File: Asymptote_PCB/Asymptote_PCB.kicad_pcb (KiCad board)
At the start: 2 copper layers, 241.3 x 74.6 mm, 107 parts, among them J1 XIAO nrf52840, J4 Conn_01x03_Female, J5 Conn_01x02_Female, SW1 MX_SW_solder, SW10 MX_SW_solder, SW11 MX_SW_solder, SW12 MX_SW_solder, SW13 MX_SW_solder, SW14 MX_SW_solder, SW15 MX_SW_solder, SW16 MX_SW_solder, SW17 MX_SW_solder, SW18 MX_SW_solder, SW19 MX_SW_solder, SW2 MX_SW_solder, SW20 MX_SW_solder, SW21 MX_SW_solder, SW22 MX_SW_solder, SW23 MX_SW_solder, SW24 MX_SW_solder, SW25 MX_SW_solder, SW26 MX_SW_solder, SW27 MX_SW_solder, SW28 MX_SW_solder, SW29 MX_SW_solder, SW3 MX_SW_solder, SW30 MX_SW_solder, SW31 MX_SW_solder, SW32 MX_SW_solder, SW33 MX_SW_solder, SW34 MX_SW_solder, SW35 MX_SW_solder, SW36 MX_SW_solder, SW37 MX_SW_solder, SW38 MX_SW_solder, SW39 MX_SW_solder, SW4 MX_SW_solder, SW40 MX_SW_solder, SW41 MX_SW_solder, SW42 MX_SW_solder, SW43 MX_SW_solder, SW44 MX_SW_solder, SW45 MX_SW_solder, SW46 MX_SW_solder, SW47 MX_SW_solder, SW48 MX_SW_solder, SW49 MX_SW_solder, SW5 MX_SW_solder, SW50 MX_SW_solder, SW51 MX_SW_solder, SW6 MX_SW_solder, SW7 MX_SW_solder, SW8 MX_SW_solder, SW9 MX_SW_solder

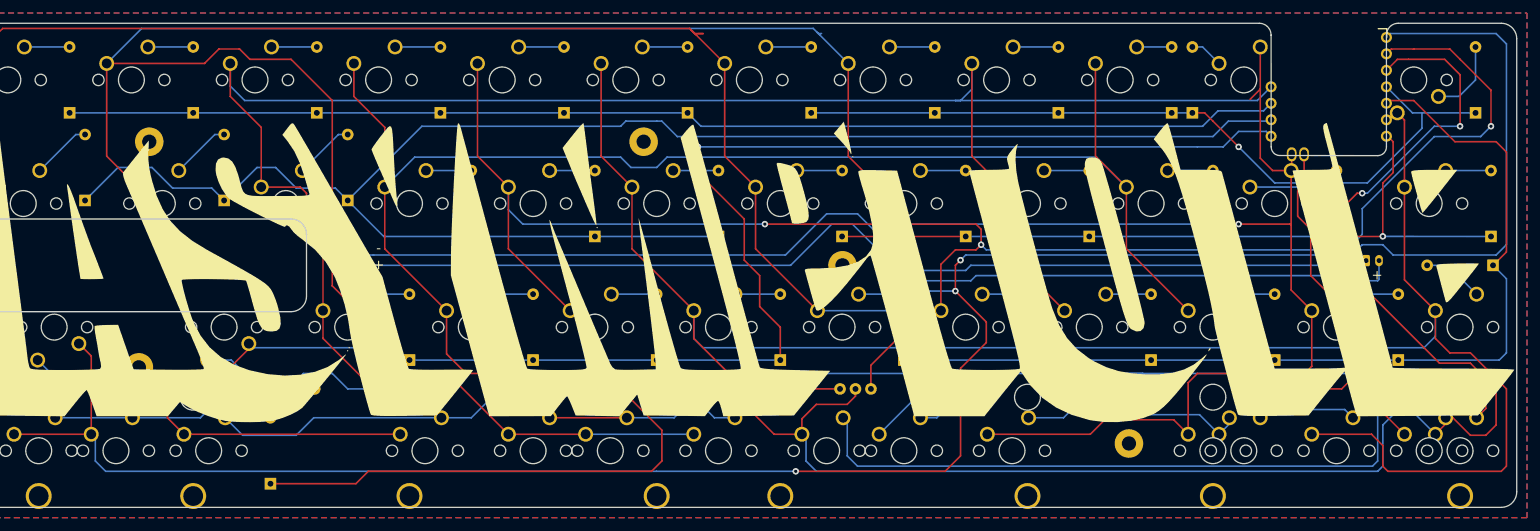
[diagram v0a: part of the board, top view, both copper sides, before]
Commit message: Added 7u stab holes, V2 Gerbers
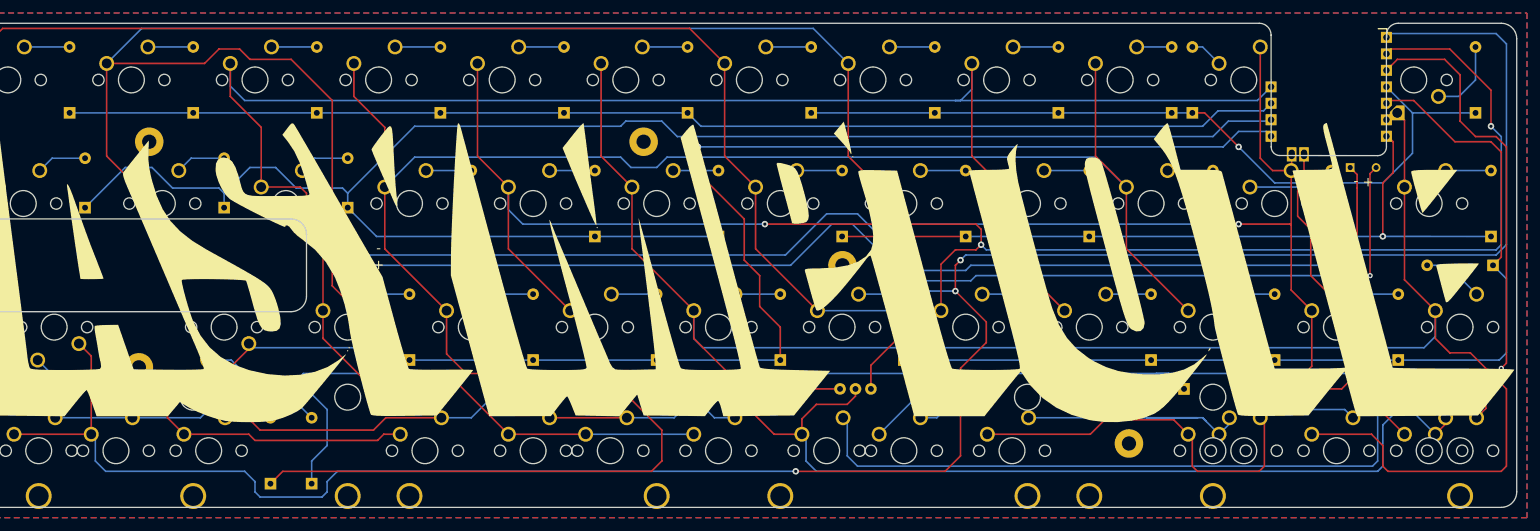
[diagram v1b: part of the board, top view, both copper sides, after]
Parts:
- added S5: MX_stab, marbastlib-mx:STAB_MX_P_7u, F.Cu at (144.5, 109.5)
- D13, D14, D15: footprint Diode_THT:D_A-405_P10.16mm_Horizontal -> Diode_THT:D_A-405_P7.62mm_Horizontal
- J4: footprint Connector_JST:JST_PH_S3B-PH-K_1x03_P2.00mm_Horizontal -> Connector_PinHeader_2.00mm:PinHeader_1x03_P2.00mm_Vertical
- J5: footprint Connector_JST:JST_PH_S2B-PH-K_1x02_P2.00mm_Horizontal -> Connector_PinHeader_2.00mm:PinHeader_1x03_P2.00mm_Vertical
- moved D26 18.1 mm to (81.8, 114.6), turned to 90 degrees
- moved J5 14.5 mm to (241.8, 65.9), turned to -90 degrees
- moved J4 5.38 mm to (86.5, 78.2), turned to 180 degrees
- moved D41 3.97 mm to (216.2, 100.0)
- moved D13 1.11 mm to (46.8, 72.1)
- moved D14 1.11 mm to (68.3, 72.1)
- moved D15 1.11 mm to (87.3, 72.1)
- moved D23 0.79 mm to (238.9, 76.5)
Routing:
- net COL3: track 503.7 -> 477.2 mm, vias 2 -> 1
- net ROW4: track 207.5 -> 225.2 mm
- net +BATT: track 168.8 -> 182.5 mm, vias 0 -> 1
- net ROW6: track 307.9 -> 296.0 mm
- net Net-(D41-A): track 37.3 -> 47.5 mm
- net COL1: track 485.0 -> 494.0 mm
- net -BATT: track 170.9 -> 179.0 mm, vias 0 -> 1
- net COL4: track 297.6 -> 292.6 mm
- net ROW2: track 257.8 -> 260.1 mm
- net ROW5: track 148.0 -> 146.2 mm
- net Net-(D14-A): track 9.29 -> 7.77 mm
- net Net-(D15-A): track 9.29 -> 7.77 mm
- net Net-(D13-A): track 9.29 -> 7.77 mm
- net Net-(D40-A): track 135.8 -> 134.9 mm
- net ROW1: track 119.9 -> 120.7 mm
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- added copper zone on B.Cu, net -BATT
- added copper zone on F.Cu, net -BATT
- removed copper zone on B.Cu, net (none)
- removed copper zone on F.Cu, net (none)
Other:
- board text added: "V2"
